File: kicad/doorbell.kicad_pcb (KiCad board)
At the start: 4 copper layers, 35.6 x 47.5 mm, 35 parts, among them J1 USB-C (USB4085), J2 WF26 (6-way screw), K1 G6K-2F-Y 4.5V, K2 G6K-2F-Y 4.5V, Q1 2N7002, Q2 2N7002, SW1 BOOT, SW2 EN, U1 ESP32-C3-MINI-1, U2 SGM2212-3.3

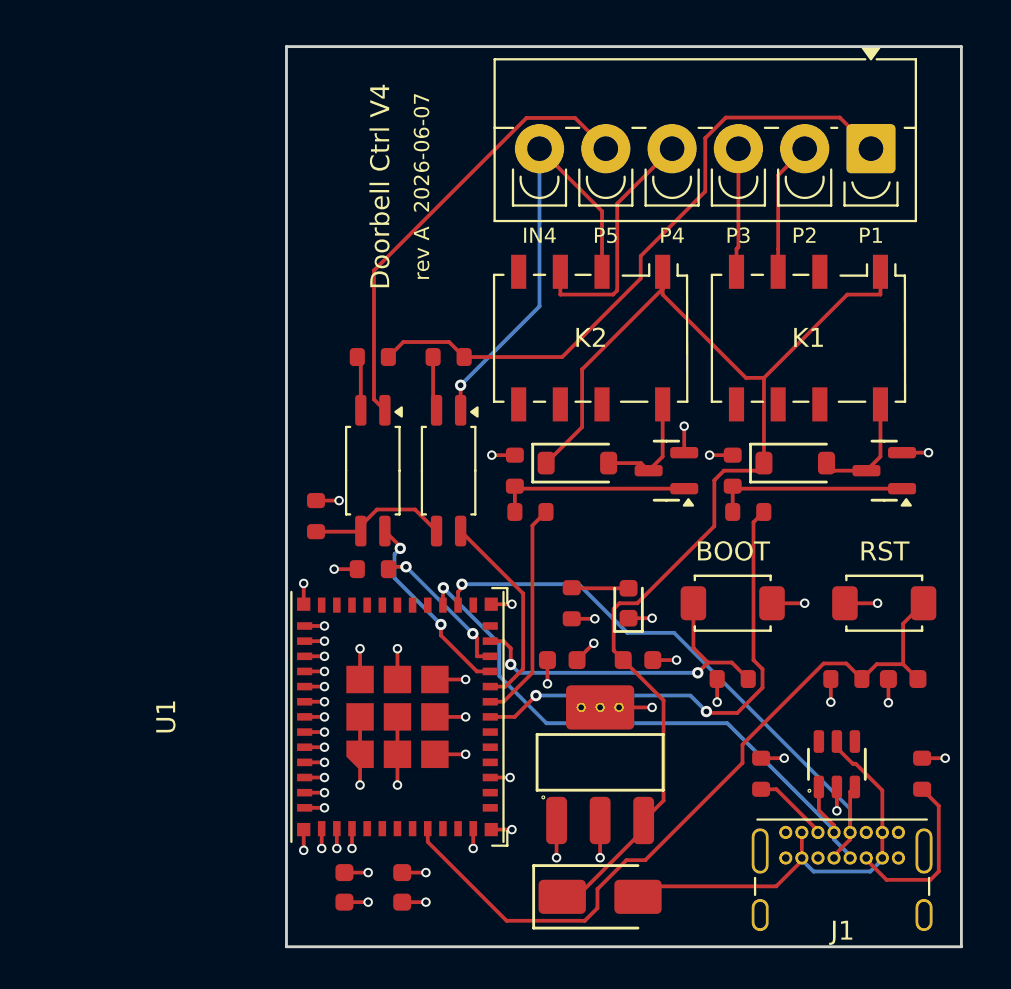
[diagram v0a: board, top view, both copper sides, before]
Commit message: Swap inner planes to In1=+3V3 / In2=GND so B.Cu references GND
Puts the GND plane adjacent to B.Cu, where the USB D+/D- pair predominantly
routes (~85% B.Cu). Before, B.Cu sat over the +3V3 plane, so the pair was mostly
+3V3-referenced; now it's GND-referenced. The other signals are slow/DC and don't
care, and +3V3 distribution is unchanged (both planes still solid). Review finding 3.

- gen_pcb.py: add_plane()/PLANE_OF swapped; stitch vias retarget by net (through-vias,
  no geometry change). ERC 0 err, DRC 0/0, check_pcb PASS.
- DESIGN.md / kicad/README.md: stackup now F.Cu / +3V3 / GND / B.Cu; finding 3 mitigated.

Note: for a guaranteed clean, coupled pair, hand-route + lock D+/D- on B.Cu in the
KiCad GUI (the codegen autoroute leaves them un-pinned). FS USB (12 Mbps) is forgiving.
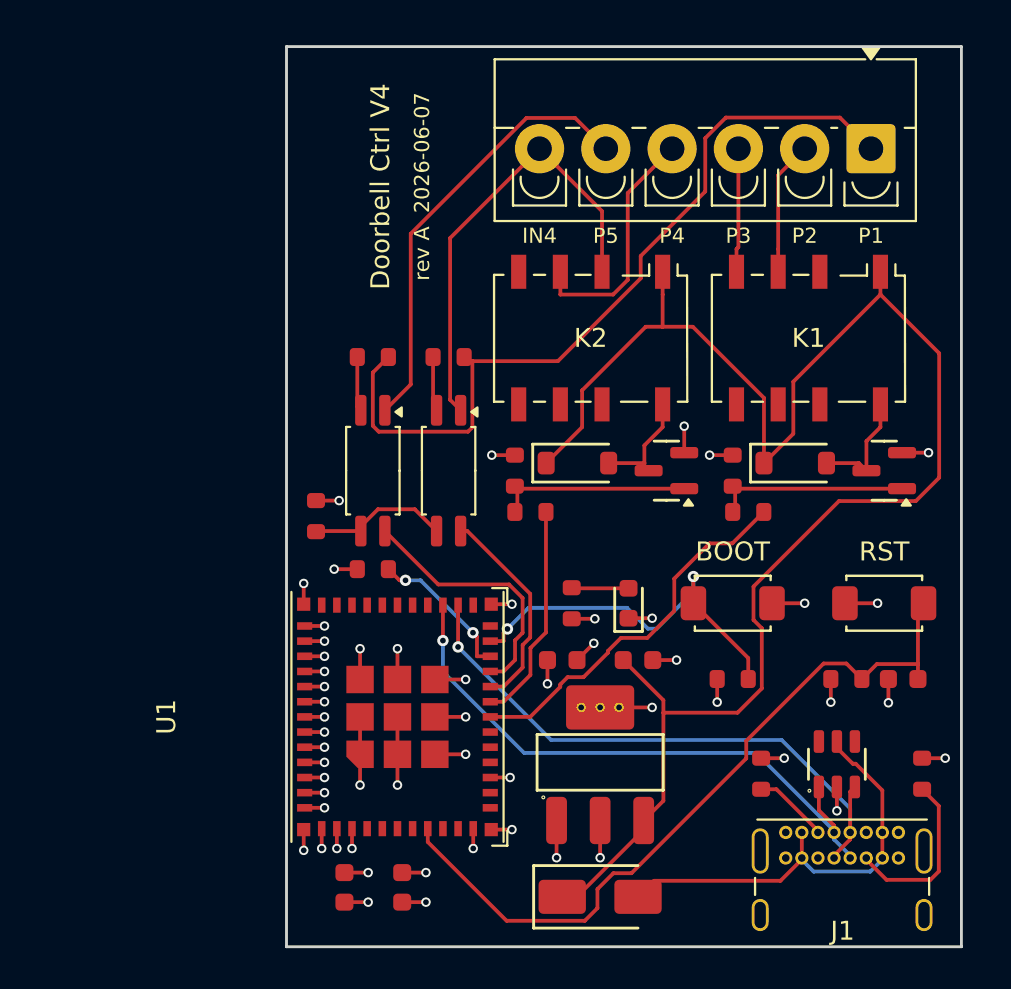
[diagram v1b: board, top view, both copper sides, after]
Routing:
- net +5V: track 65.3 -> 86.6 mm
- net P1: track 34.4 -> 42.9 mm
- net GATE1_DRV: track 25.5 -> 20.1 mm, vias 2 -> 0
- net OC2_OUT: track 10.4 -> 13.7 mm, vias 2 -> 0
- net BOOT: track 18.8 -> 20.4 mm
- net IN_P4: track 23.4 -> 23.9 mm, vias 1 -> 0
- added copper zone on In1.Cu, net +3V3
- added copper zone on In2.Cu, net GND
- removed copper zone on In2.Cu, net +3V3
- removed copper zone on In1.Cu, net GND

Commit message: EN reset cap 100nF -> 1µF; add ESP32 PCB best-practices review
- C_en bumped to 1µF, Espressif's EN-RC spec value (was 100nF). Regenerated
  schematic/PCB/fab: ERC 0, DRC 0/0, 0 unconnected, check_pcb PASS.
- Add docs/ESP32_PCB_BEST_PRACTICES.md: sourced ESP32-C3 (module) PCB
  best-practices checklist + line-by-line comparison against V4.
- Sync DESIGN.md BOM: U2 is the SGM2212-3.3 LDO (was a stale AMS1117-3.3
  line) — matches the decisions/power-tree/review sections.
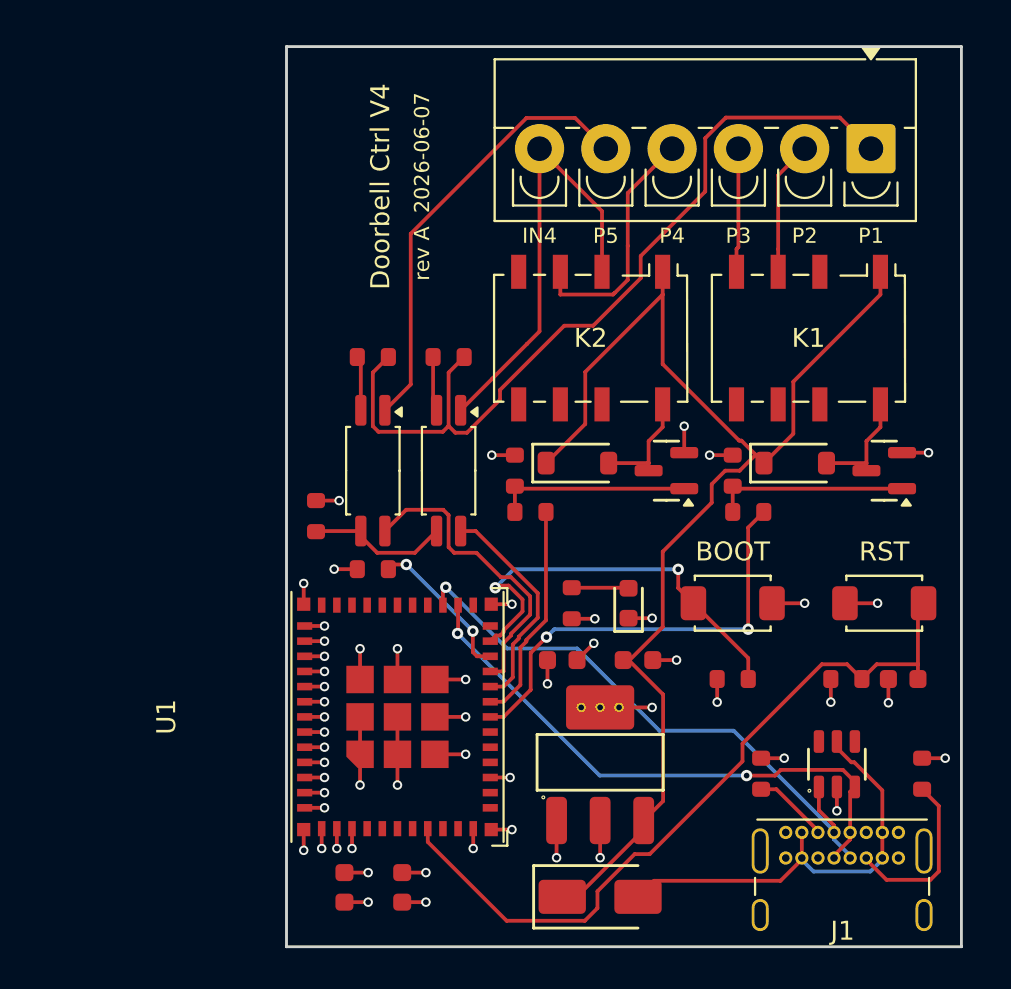
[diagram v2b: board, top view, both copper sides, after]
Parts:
- C5: value 100nF -> 1uF
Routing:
- net +5V: track 86.6 -> 66.8 mm
- net GATE1_DRV: track 20.1 -> 23.2 mm, vias 0 -> 2
- net OC2_OUT: track 13.7 -> 16.3 mm
- net P1: track 42.9 -> 44.9 mm
- net BOOT: track 20.4 -> 22.2 mm
- net USB_DM: track 31.9 -> 30.5 mm, vias 1 -> 2
- net USB_DP: track 32.2 -> 31.3 mm
- net OC1_OUT: track 11.2 -> 11.8 mm

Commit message: Add 3 PCBA fiducials (body-aware placement, BOM/CPL-excluded)
Three global optical reference marks (Fiducial_1mm_Mask2mm) added in
gen_pcb.py after plane-stitching, forming an asymmetric triangle so the
pick-and-place camera can resolve board orientation.

Placement is body-aware: the search clears every component COURTYARD by
>=1.4mm (not just pads), so a mark never lands under a part. An earlier
pad-only check tucked a fiducial into the gap between J1's USB-C pad rows
(under the connector shell); the courtyard check fixes that and the
fiducial courtyard is kept so DRC courtyard-overlap guards regressions.

Other gotchas handled to keep DRC 0/0:
- FP_EXCLUDE_FROM_POS_FILES + FP_EXCLUDE_FROM_BOM so fiducials stay out of
  the CPL/BOM; jlcpcb_cpl.py and check_pcb.py honour the attribute.
- Drop the stock pad's 0.6mm local clearance override (Freerouting/DSN
  ignores it on a netless pad), inheriting the 0.2mm board default.
- Minimal F.Cu-only keepout (r=1.1mm) per fiducial so an autorouted track
  can't cross the mask window and bridge it; B.Cu/inner planes stay free
  so routing still completes 0 unrouted.

Board packing leaves the right third with no >=1.4mm-clear spot, so marks
land top-left / bottom-left / bottom-centre (documented in DESIGN.md).
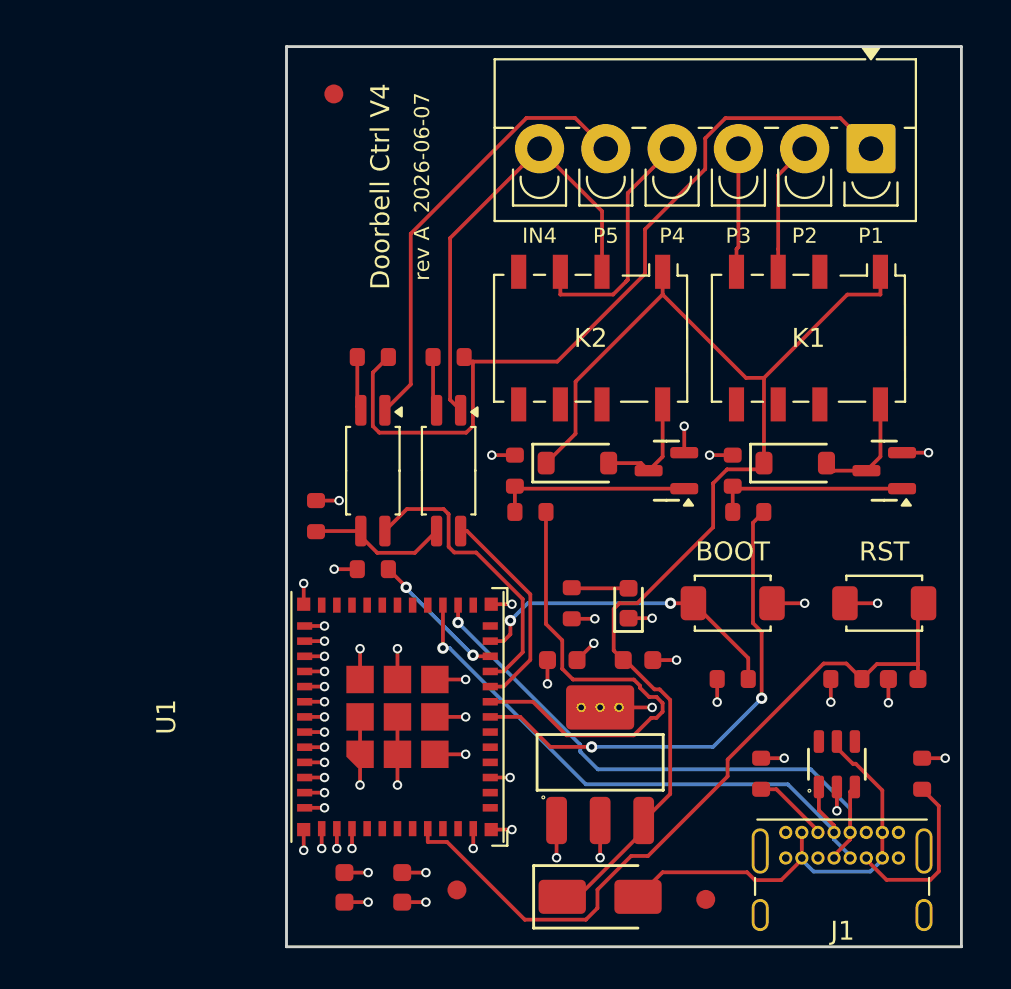
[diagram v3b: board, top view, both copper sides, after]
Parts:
- added FID1: FID, Fiducial_1mm_Mask2mm, F.Cu at (1.94, 14.1)
- added FID2: FID, Fiducial_1mm_Mask2mm, F.Cu at (8.44, 56.1)
- added FID3: FID, Fiducial_1mm_Mask2mm, F.Cu at (21.6, 56.6)
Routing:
- net GATE2_DRV: track 11.6 -> 25.6 mm
- net BOOT: track 22.2 -> 17.2 mm
- net GATE1_DRV: track 23.2 -> 26.3 mm
- net P1: track 44.9 -> 42.9 mm
- net +5V: track 66.8 -> 65.5 mm
- net USB_DM: track 30.5 -> 31.4 mm, vias 2 -> 1
- net GPIO8: track 8.14 -> 7.33 mm
- net OC1_OUT: track 11.8 -> 11.2 mm
- net OC2_OUT: track 16.3 -> 15.7 mm

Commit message: Place R3 (R_em) south of OK1, rotated CW 90°->0°
Move the shared opto emitter resistor from left-of-OC2 (1,36.4,90) into
the OK1<->U1 gap directly south of OK1 (8,39.2,0). Re-routed; DRC 0/0,
check_pcb PASS, fiducials re-placed clean.
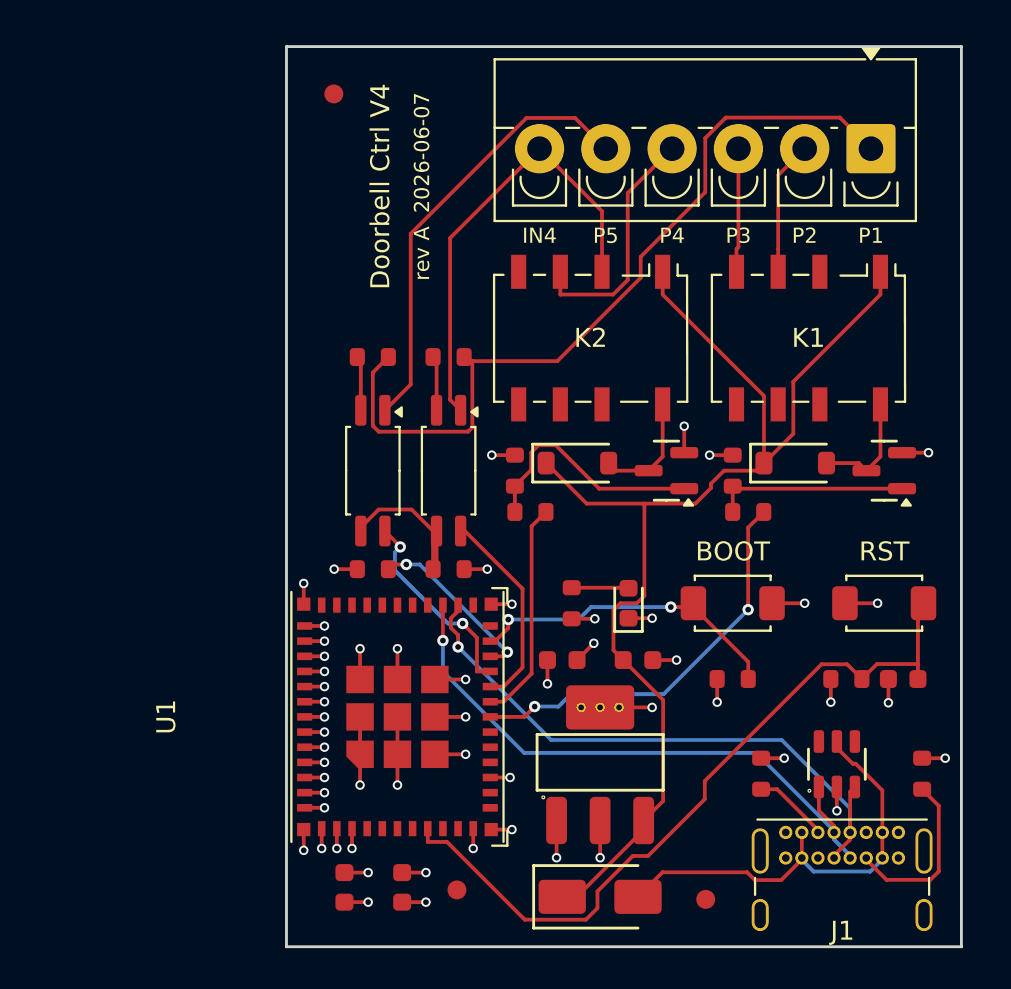
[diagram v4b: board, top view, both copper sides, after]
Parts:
- moved R3 7.54 mm to (8.00, 39.2), turned to 0 degrees
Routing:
- net GATE2_DRV: track 25.6 -> 11.6 mm
- net OC2_OUT: track 15.7 -> 10.8 mm, vias 0 -> 2
- net GATE1_DRV: track 26.3 -> 21.5 mm
- net GATE2: track 10.3 -> 12.7 mm
- net GPIO8: track 7.33 -> 9.31 mm
- net OC_EMIT: track 7.49 -> 8.97 mm
- net +5V: track 65.5 -> 64.1 mm
- net USB_DM: track 31.4 -> 32.2 mm
- net USB_DP: track 31.4 -> 32.2 mm

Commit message: Swap U1 to ESP32-C3-WROOM-02-N4 (Economic PCBA) + re-floorplan upper-left
The ESP32-C3-MINI-1 is Standard-PCBA-only at JLCPCB, forcing the $25/side
setup. The ESP32-C3-WROOM-02-N4 (LCSC C2934560) is Economic-eligible and
the same C3 SoC, so the ESPHome config is unchanged.

Not a drop-in: WROOM-02 is larger (18x20 vs 13.2x16.6) with a different
pad map, so every U1 net was remapped (3V3 3->1, EN 8->2, IO4 18->3,
IO5 19->4, IO6 20->5, IO7 21->6, IO8 22->7, IO9 23->8, USB D-/D+ 26/27->
13/14, GND -> pins 9 + EPAD 19) and NOCONN updated to the unused WROOM-02
GPIOs. EDGE_OVERHANG retuned to 5.9mm: antenna still overhangs the left
edge, pins 1/18 now sit ~1.5mm inside instead of 0.5mm.

Re-floorplanned the upper-left for the bigger module (directed):
- opto sub-assembly (OC1/OC2, R_lim1/2, R_em) centered in the UL quadrant
- U1 up 5mm to clear the C3/C6 decoupling caps
- R10 moved out from under U1 to the right of C3 (rotated CCW)
- C6/C3/R10 nudged up 0.5mm
- product-name / rev silk relocated to the strip left of the optos

Routes 0 unrouted, DRC 0/0, check_pcb PASS. Adds the WROOM-02 datasheet.
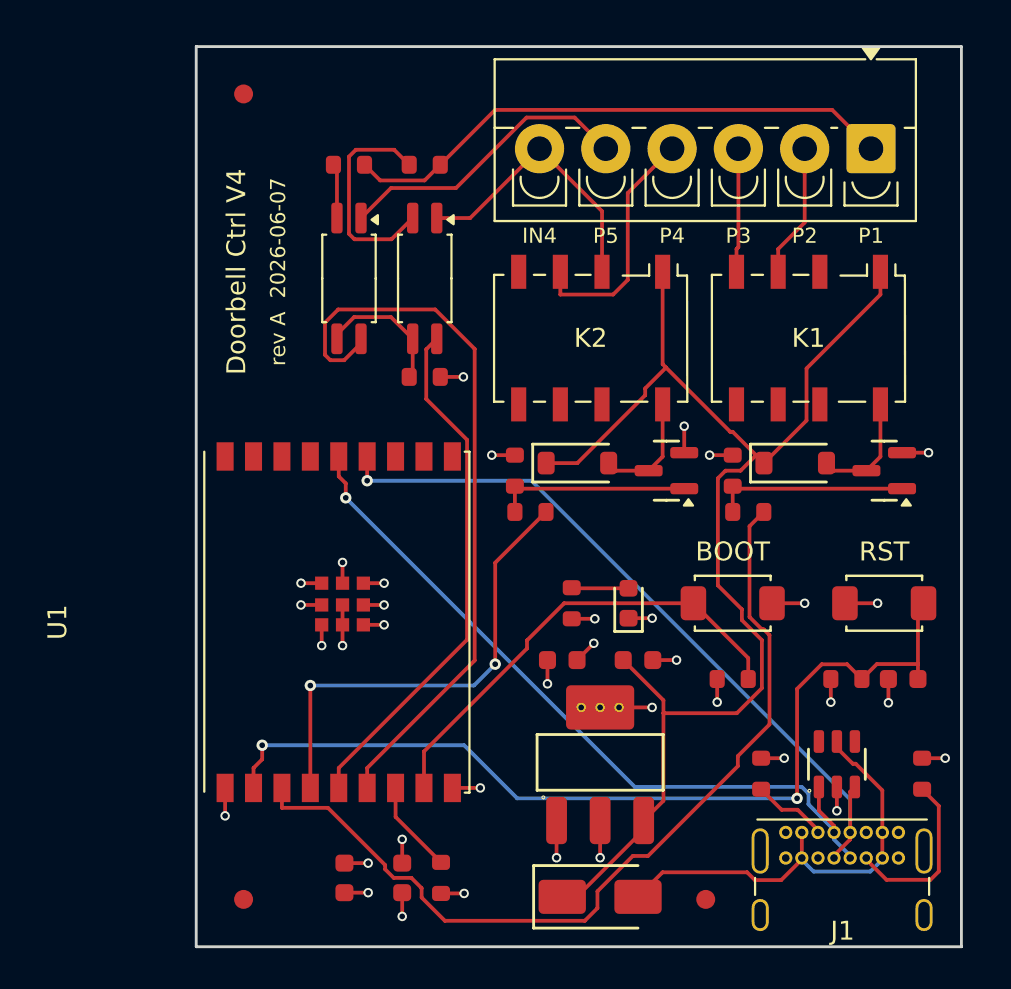
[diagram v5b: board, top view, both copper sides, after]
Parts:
- U1: value ESP32-C3-MINI-1 -> ESP32-C3-WROOM-02-N4; footprint ESP32-C3-MINI-1 -> ESP32-C3-WROOM-02
- moved R10 16.7 mm to (7.60, 55.5), turned to -90 degrees
- moved FID2 11.3 mm to (-2.83, 56.6)
- moved R3 10.2 mm to (6.74, 29.1)
- moved OK1 10.2 mm to (6.74, 23.9)
- moved OK2 10.2 mm to (2.74, 23.9)
- moved R1 10.2 mm to (6.74, 17.9)
- moved R2 10.2 mm to (2.74, 17.9)
- moved U1 5.02 mm to (2.10, 42.0)
- moved FID1 4.77 mm to (-2.83, 14.1)
- moved C3 0.50 mm to (5.55, 55.5)
- moved C6 0.50 mm to (2.50, 55.5)
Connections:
- U1 pad 1: GND -> +3V3
- U1 pad 11: GND -> (no net)
- U1 pad 13: (no net) -> USB_DM
- U1 pad 14: GND -> USB_DP
- U1 pad 18: GATE1_DRV -> (no net)
- U1 pad 19: GATE2_DRV -> GND
- U1 pad 2: GND -> EN
- U1 pad 3: +3V3 -> GATE1_DRV
- U1 pad 4: (no net) -> GATE2_DRV
- U1 pad 5: (no net) -> OC1_OUT
- U1 pad 6: (no net) -> OC2_OUT
- U1 pad 7: (no net) -> GPIO8
- U1 pad 8: EN -> BOOT
- U1 pad 9: (no net) -> GND
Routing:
- net OC2_OUT: track 10.8 -> 38.9 mm, vias 2 -> 0
- net GND: track 60.6 -> 34.4 mm, vias 45 -> 26
- net GATE1_DRV: track 21.5 -> 46.8 mm, vias 2 -> 0
- net OC1_OUT: track 10.8 -> 27.6 mm
- net P1: track 42.8 -> 29.5 mm
- net GATE2_DRV: track 11.6 -> 24.8 mm, vias 0 -> 2
- net EN: track 39.7 -> 49.3 mm, vias 0 -> 2
- net IN_P4: track 23.9 -> 14.8 mm
- net OC1_CATH: track 2.89 -> 11.7 mm
- net USB_DP: track 32.2 -> 40.3 mm
- net BOOT: track 16.9 -> 24.8 mm, vias 2 -> 0
- net P5: track 23.4 -> 15.8 mm
- net USB_DM: track 32.2 -> 39.7 mm
- net +5V: track 64.1 -> 70.0 mm
- net GPIO8: track 9.31 -> 4.92 mm, vias 2 -> 0
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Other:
- board size 35.6 x 47.5 mm -> 40.4 x 47.5 mm
